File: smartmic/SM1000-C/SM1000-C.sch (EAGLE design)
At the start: 199 parts, among them CN1 HDR100-3, CN10 ST-3509, CN11 HDR100-3, CN12 DF11-16DS, CN2 MOLEX-MINI-B-SMT, CN3 RASM722PX, CN4 RJ-45, CN5 ST-3509, CN6 ST-3509, CN7 ST-3509, CN8 ST-3509, CN9 ST-3509, J1 JMP-2PIN, J3 JMP-2PIN, J4 JMP-2PIN, P1 TPAD50, P10 TPAD50, P11 TPAD50, P12 TPAD50, P13 TPAD50, P14 TPAD50, P15 TPAD50, P16 TPAD50, P17 TPAD50, P18 TPAD50, P19 TPAD50, P2 TPAD50, P20 TPAD50, P3 TPAD50, P4 TPAD50, P5 TPAD50, P6 TPAD50, P7 TPAD50, P8 TPAD50, P9 TPAD50, SW1 SW-BOURNS-7914S, SW2 SW-BOURNS-7914S, SW3 DPDT, SW4 SW-BOURNS-7914S, SW5 SW-BOURNS-7914J, T1 SM-LP-5001, T2 SM-LP-5001, U1 STM32F405, U2 LD3985M33R, U3 STMPS2141, U4 EMIF02-USB03F2, U5 TPS54329E, U6 LMV341, U7 LMV341, U8 LM386M-1, U9 LMV341

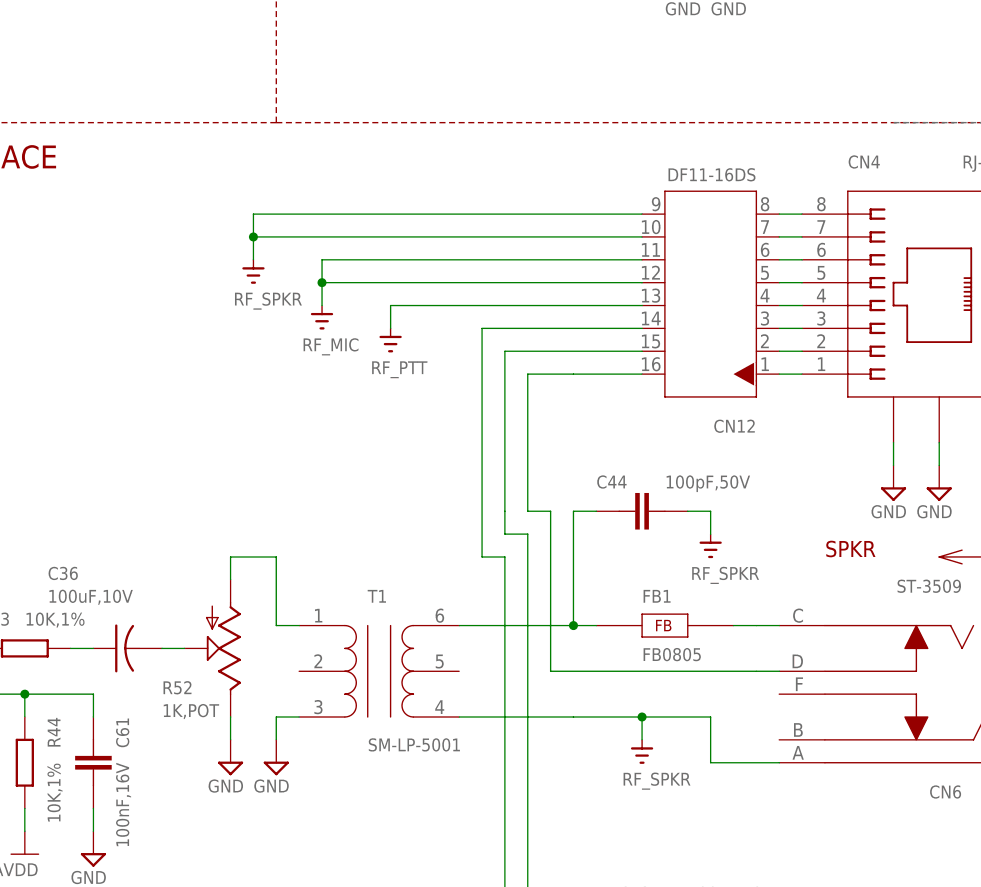
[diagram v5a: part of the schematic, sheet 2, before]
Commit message: 10/24/2014 Update to Schematic, BOM & PCB - 10/24/2014  RGB Add Panasonic POTs Add Hirose A3C-16DA 2 x 8 female box header. Note: ST-3509 3.5mm connector cost unknown. Parts yet to be selected show $0.00 cost. Still need PTT switch selection.
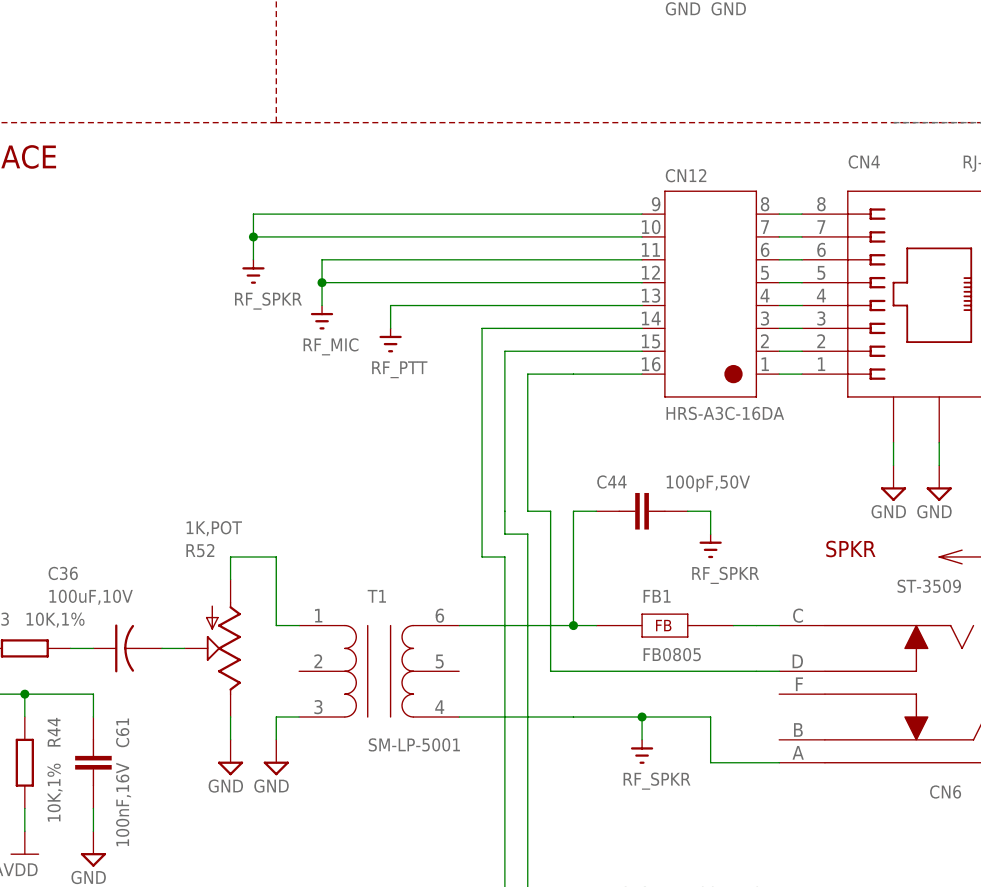
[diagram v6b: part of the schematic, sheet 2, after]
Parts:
- CN12: value DF11-16DS -> HRS-A3C-16DA; device SM1000:HRS-DF11-16DS -> _RoweTel:HRS-A3C-16DA
- R42, R47, R52: device _RoweTel:POT3361 -> _RoweTel:PAN-EVM1D
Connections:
- net SPKR: now also CN12.P16; no longer CN12.16
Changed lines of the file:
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@@
 <part name="LED8" library="_Coherix" deviceset="LTST-C" device="" value="LED-RED,RA"/>
 <part name="V58" library="A-SUPPLY2" deviceset="GND" device=""/>
-<part name="CN12" library="SM1000" deviceset="HRS-DF11-16DS" device="" value="DF11-16DS"/>
 <part name="LD2" library="_RoweTel" deviceset="LTV-817S" device=""/>
 <part name="R51" library="AA-ipc-7351-resistor" deviceset="RESISTOR_" device="0603" value="390,1%"/>
@@
 <part name="PCB1" library="_Coherix" deviceset="PCB" device="" value="SM1000C"/>
 <part name="V1" library="A-SUPPLY2" deviceset="GND" device=""/>
-<part name="R47" library="_RoweTel" deviceset="POT3361" device="" value="500,POT"/>
-<part name="R52" library="_RoweTel" deviceset="POT3361" device="" value="1K,POT"/>
+<part name="R47" library="_RoweTel" deviceset="PAN-EVM1D" device="" value="500,POT"/>
+<part name="R52" library="_RoweTel" deviceset="PAN-EVM1D" device="" value="1K,POT"/>
 <part name="C22" library="AA-ipc-7351-capacitor" deviceset="CAPACITOR_" device="0603" value="100nF,16V"/>
 <part name="C23" library="AA-ipc-7351-capacitor" deviceset="CAPACITOR_" device="0603" value="100nF,25V"/>
@@
 <part name="U9" library="_RoweTel" deviceset="LMV341" device=""/>
 <part name="R41" library="AA-ipc-7351-resistor" deviceset="RESISTOR_" device="0603" value="2.2K,1%"/>
-<part name="R42" library="_RoweTel" deviceset="POT3361" device="" value="500K,POT"/>
+<part name="R42" library="_RoweTel" deviceset="PAN-EVM1D" device="" value="500K,POT"/>
 <part name="V62" library="A-SUPPLY2" deviceset="GND" device=""/>
 <part name="R53" library="AA-ipc-7351-resistor" deviceset="RESISTOR_" device="0603" value="2.2K,1%"/>
@@
 <part name="CN9" library="_RoweTel" deviceset="ST-3509" device=""/>
 <part name="CN10" library="_RoweTel" deviceset="ST-3509" device=""/>
+<part name="CN12" library="_RoweTel" deviceset="HRS-A3C-16DA" device=""/>
 </parts>
 <sheets>
@@
 <attribute name="VALUE" x="246.38" y="215.138" size="1.4224" layer="96" ratio="9"/>
 </instance>
-<instance part="CN12" gate="G$1" x="317.5" y="180.34" smashed="yes" rot="R180">
-<attribute name="NAME" x="322.58" y="167.64" size="1.4224" layer="95" ratio="10" rot="R180"/>
-<attribute name="VALUE" x="322.58" y="195.58" size="1.4224" layer="96" ratio="10" rot="R180"/>
-</instance>
 <instance part="LD2" gate="G$1" x="279.4" y="60.96" smashed="yes">
 <attribute name="NAME" x="272.415" y="66.675" size="1.778" layer="95"/>
@@
 </instance>
 <instance part="R52" gate="G$1" x="264.16" y="142.24" smashed="yes" rot="R180">
-<attribute name="NAME" x="256.54" y="137.16" size="1.4224" layer="95" ratio="9"/>
-<attribute name="VALUE" x="256.54" y="134.62" size="1.4224" layer="96" ratio="9"/>
+<attribute name="NAME" x="259.08" y="152.4" size="1.4224" layer="95" ratio="9"/>
+<attribute name="VALUE" x="259.08" y="154.94" size="1.4224" layer="96" ratio="9"/>
 </instance>
 <instance part="C22" gate="G$1" x="124.46" y="175.26" smashed="yes" rot="R270">
@@
 </instance>
 <instance part="CN10" gate="G$1" x="307.34" y="228.6" rot="MR180"/>
+<instance part="CN12" gate="G$1" x="317.5" y="180.34" smashed="yes">
+<attribute name="NAME" x="312.42" y="194.056" size="1.4224" layer="95" ratio="10"/>
+<attribute name="VALUE" x="312.42" y="167.64" size="1.4224" layer="96" ratio="10"/>
+</instance>
 </instances>
 <busses>
@@
 <net name="N$51" class="0">
 <segment>
-<pinref part="CN12" gate="G$1" pin="8"/>
 <pinref part="CN4" gate="G$1" pin="8"/>
 <wire x1="327.66" y1="190.5" x2="325.12" y2="190.5" width="0.1524" layer="91"/>
+<pinref part="CN12" gate="G$1" pin="8"/>
 </segment>
 </net>
 <net name="N$52" class="0">
 <segment>
-<pinref part="CN12" gate="G$1" pin="7"/>
 <pinref part="CN4" gate="G$1" pin="7"/>
 <wire x1="327.66" y1="187.96" x2="325.12" y2="187.96" width="0.1524" layer="91"/>
+<pinref part="CN12" gate="G$1" pin="7"/>
 </segment>
 </net>
 <net name="N$53" class="0">
 <segment>
-<pinref part="CN12" gate="G$1" pin="6"/>
 <pinref part="CN4" gate="G$1" pin="6"/>
 <wire x1="327.66" y1="185.42" x2="325.12" y2="185.42" width="0.1524" layer="91"/>
+<pinref part="CN12" gate="G$1" pin="6"/>
 </segment>
 </net>
 <net name="N$54" class="0">
 <segment>
-<pinref part="CN12" gate="G$1" pin="5"/>
 <pinref part="CN4" gate="G$1" pin="5"/>
 <wire x1="327.66" y1="182.88" x2="325.12" y2="182.88" width="0.1524" layer="91"/>
+<pinref part="CN12" gate="G$1" pin="5"/>
 </segment>
 </net>
 <net name="N$55" class="0">
 <segment>
-<pinref part="CN12" gate="G$1" pin="4"/>
 <pinref part="CN4" gate="G$1" pin="4"/>
 <wire x1="327.66" y1="180.34" x2="325.12" y2="180.34" width="0.1524" layer="91"/>
+<pinref part="CN12" gate="G$1" pin="4"/>
 </segment>
 </net>
 <net name="N$56" class="0">
 <segment>
-<pinref part="CN12" gate="G$1" pin="3"/>
 <pinref part="CN4" gate="G$1" pin="3"/>
 <wire x1="327.66" y1="177.8" x2="325.12" y2="177.8" width="0.1524" layer="91"/>
+<pinref part="CN12" gate="G$1" pin="3"/>
 </segment>
 </net>
 <net name="N$57" class="0">
 <segment>
-<pinref part="CN12" gate="G$1" pin="2"/>
 <pinref part="CN4" gate="G$1" pin="2"/>
 <wire x1="327.66" y1="175.26" x2="325.12" y2="175.26" width="0.1524" layer="91"/>
+<pinref part="CN12" gate="G$1" pin="2"/>
 </segment>
 </net>
 <net name="N$58" class="0">
 <segment>
-<pinref part="CN12" gate="G$1" pin="1"/>
 <pinref part="CN4" gate="G$1" pin="1"/>
 <wire x1="327.66" y1="172.72" x2="325.12" y2="172.72" width="0.1524" layer="91"/>
+<pinref part="CN12" gate="G$1" pin="1"/>
 </segment>
 </net>
@@
 <wire x1="294.64" y1="154.94" x2="294.64" y2="157.48" width="0.1524" layer="91"/>
 <wire x1="294.64" y1="157.48" x2="294.64" y2="175.26" width="0.1524" layer="91"/>
-<pinref part="CN12" gate="G$1" pin="15"/>
 <wire x1="294.64" y1="175.26" x2="309.88" y2="175.26" width="0.1524" layer="91"/>
 <wire x1="297.18" y1="93.98" x2="325.12" y2="93.98" width="0.1524" layer="91"/>
 <pinref part="CN7" gate="G$1" pin="D"/>
 <wire x1="325.12" y1="93.98" x2="332.74" y2="93.98" width="0.1524" layer="91"/>
+<pinref part="CN12" gate="G$1" pin="15"/>
 </segment>
 </net>
@@
 <wire x1="299.72" y1="157.48" x2="297.18" y2="157.48" width="0.1524" layer="91"/>
 <wire x1="297.18" y1="157.48" x2="297.18" y2="172.72" width="0.1524" layer="91"/>
-<pinref part="CN12" gate="G$1" pin="16"/>
 <wire x1="309.88" y1="172.72" x2="302.26" y2="172.72" width="0.1524" layer="91"/>
 <wire x1="297.18" y1="172.72" x2="302.26" y2="172.72" width="0.1524" layer="91"/>
 <wire x1="322.58" y1="139.7" x2="325.12" y2="139.7" width="0.1524" layer="91"/>
 <pinref part="CN6" gate="G$1" pin="D"/>
+<pinref part="CN12" gate="G$1" pin="P16"/>
 </segment>
 </net>
@@
 <wire x1="294.64" y1="58.42" x2="332.74" y2="58.42" width="0.1524" layer="91"/>
 <wire x1="294.64" y1="152.4" x2="292.1" y2="152.4" width="0.1524" layer="91"/>
-<pinref part="CN12" gate="G$1" pin="14"/>
 <wire x1="294.64" y1="177.8" x2="309.88" y2="177.8" width="0.1524" layer="91"/>
 <wire x1="292.1" y1="177.8" x2="294.64" y2="177.8" width="0.1524" layer="91"/>
 <wire x1="292.1" y1="152.4" x2="292.1" y2="177.8" width="0.1524" layer="91"/>
 <pinref part="CN9" gate="G$1" pin="D"/>
+<pinref part="CN12" gate="G$1" pin="14"/>
 </segment>
 </net>
@@
 </segment>
 <segment>
-<pinref part="CN12" gate="G$1" pin="11"/>
 <wire x1="309.88" y1="185.42" x2="274.32" y2="185.42" width="0.1524" layer="91"/>
 <wire x1="274.32" y1="185.42" x2="274.32" y2="182.88" width="0.1524" layer="91"/>
-<pinref part="CN12" gate="G$1" pin="12"/>
 <wire x1="274.32" y1="182.88" x2="274.32" y2="180.34" width="0.1524" layer="91"/>
 <wire x1="309.88" y1="182.88" x2="274.32" y2="182.88" width="0.1524" layer="91"/>
 <junction x="274.32" y="182.88"/>
 <pinref part="V133" gate="G$1" pin="RF_MIC"/>
+<pinref part="CN12" gate="G$1" pin="11"/>
+<pinref part="CN12" gate="G$1" pin="12"/>
 </segment>
 </net>
@@
 </segment>
 <segment>
-<pinref part="CN12" gate="G$1" pin="9"/>
 <wire x1="309.88" y1="190.5" x2="266.7" y2="190.5" width="0.1524" layer="91"/>
 <wire x1="266.7" y1="190.5" x2="266.7" y2="187.96" width="0.1524" layer="91"/>
-<pinref part="CN12" gate="G$1" pin="10"/>
 <wire x1="266.7" y1="187.96" x2="266.7" y2="185.42" width="0.1524" layer="91"/>
 <wire x1="309.88" y1="187.96" x2="266.7" y2="187.96" width="0.1524" layer="91"/>
 <junction x="266.7" y="187.96"/>
 <pinref part="V134" gate="G$1" pin="RF_SPKR"/>
+<pinref part="CN12" gate="G$1" pin="9"/>
+<pinref part="CN12" gate="G$1" pin="10"/>
 </segment>
 </net>
@@
 </segment>
 <segment>
-<pinref part="CN12" gate="G$1" pin="13"/>
 <wire x1="309.88" y1="180.34" x2="281.94" y2="180.34" width="0.1524" layer="91"/>
 <wire x1="281.94" y1="180.34" x2="281.94" y2="177.8" width="0.1524" layer="91"/>
 <pinref part="V92" gate="G$1" pin="RF_PTT"/>
+<pinref part="CN12" gate="G$1" pin="13"/>
 </segment>
 </net>
